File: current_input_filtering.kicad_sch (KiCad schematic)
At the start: 0 parts

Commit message: Launchpad controller revision 06/03/2024
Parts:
- added F14: Polyfuse, symbol Device:Polyfuse
- added J36: Conn_01x04_Socket, symbol Connector:Conn_01x04_Socket
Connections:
- net Iout: now also J36.2 (Pin_2)
- new net: F14.1, J36.1 (Pin_1)
- new net +12L: F14.2
- no-connect marks 0 -> 2
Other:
- note added: "super simple. fuse on the output to prevent damage by connecting to sketchy peripheral. sensor should drive the current, so shouldn't see too much noise => no filter required"

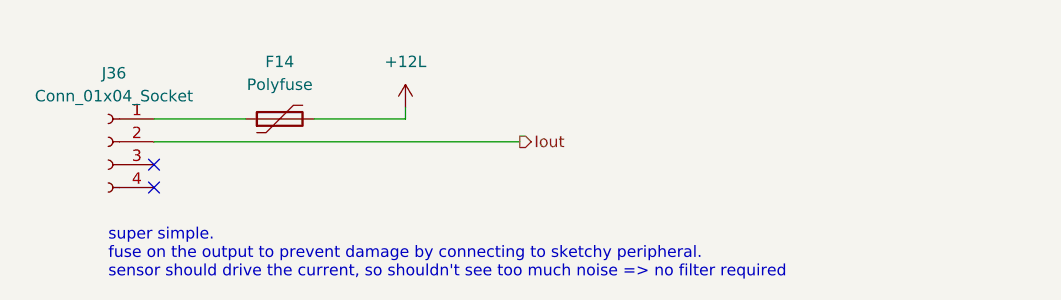
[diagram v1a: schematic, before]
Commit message: added footprints to almost all components
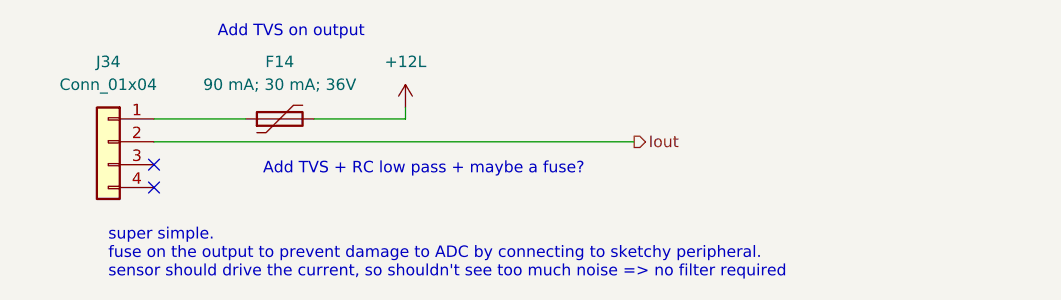
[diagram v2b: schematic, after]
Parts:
- removed J36: Conn_01x04_Socket, symbol Connector:Conn_01x04_Socket
- added J34: Conn_01x04, Connector_JST:JST_GH_BM04B-GHS-TBT_1x04-1MP_P1.25mm_Vertical, symbol Connector_Generic:Conn_01x04
- F14: value Polyfuse -> 90 mA; 30 mA; 36V; footprint (none) -> Fuse:Fuse_0805_2012Metric_Pad1.15x1.40mm_HandSolder; Mouser# (none) -> 576-0603L003/36YR
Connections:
- net Iout: now also J34.2 (Pin_2)
- net at F14.1: now also J34.1 (Pin_1)
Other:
- note added: "Add TVS + RC low pass + maybe a fuse?"
- note added: "Add TVS on output"
- note added: "super simple. fuse on the output to prevent damage to ADC by connecting to sketchy peripheral. sensor should drive the current, so shouldn't see too much noise => no filter required"
- note removed: "super simple. fuse on the output to prevent damage by connecting to sketchy peripheral. sensor should drive the current, so shouldn't see too much noise => no filter required"
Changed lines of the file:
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@@
 	(wire
 		(pts
-			(xy 100.33 60.96) (xy 59.69 60.96)
+			(xy 59.69 60.96) (xy 113.03 60.96)
 		)
 		(stroke
@@
 		)
 	)
-	(text "super simple. \nfuse on the output to prevent damage by connecting to sketchy peripheral.\nsensor should drive the current, so shouldn't see too much noise => no filter required"
+	(text "super simple. \nfuse on the output to prevent damage to ADC by connecting to sketchy peripheral.\nsensor should drive the current, so shouldn't see too much noise => no filter required"
 		(exclude_from_sim no)
 		(at 54.61 76.2 0)
@@
 		)
 	)
+	(text "Add TVS + RC low pass + maybe a fuse? "
+		(exclude_from_sim no)
+		(at 89.662 64.008 0)
+		(effects
+			(font
+				(size 1.27 1.27)
+			)
+		)
+	)
+	(text "Add TVS on output"
+		(exclude_from_sim no)
+		(at 74.93 48.768 0)
+		(effects
+			(font
+				(size 1.27 1.27)
+			)
+		)
+	)
 	(hierarchical_label "Iout"
 		(shape output)
-		(at 100.33 60.96 0)
+		(at 113.03 60.96 0)
 		(fields_autoplaced yes)
 		(effects
@@
 			)
 			(justify left)
-		)
-	)
-	(symbol
-		(lib_id "Connector:Conn_01x04_Socket")
-		(at 54.61 60.96 0)
-		(mirror y)
-		(unit 1)
-		(exclude_from_sim no)
-		(in_bom yes)
-		(on_board yes)
-		(dnp no)
-		(fields_autoplaced yes)
-		(property "Reference" "J36"
-			(at 55.245 53.34 0)
-			(effects
-				(font
-					(size 1.27 1.27)
-				)
-			)
-		)
-		(property "Value" "Conn_01x04_Socket"
-			(at 55.245 55.88 0)
-			(effects
-				(font
-					(size 1.27 1.27)
-				)
-			)
-		)
-		(property "Footprint" ""
-			(at 54.61 60.96 0)
-			(effects
-				(font
-					(size 1.27 1.27)
-				)
-				(hide yes)
-			)
-		)
-		(property "Datasheet" "~"
-			(at 54.61 60.96 0)
-			(effects
-				(font
-					(size 1.27 1.27)
-				)
-				(hide yes)
-			)
-		)
-		(property "Description" ""
-			(at 54.61 60.96 0)
-			(effects
-				(font
-					(size 1.27 1.27)
-				)
-				(hide yes)
-			)
-		)
-		(pin "1"
-		)
-		(pin "2"
-		)
-		(pin "3"
-		)
-		(pin "4"
-		)
-		(instances
-			(project "launchpad-controller-v2"
-				(path "/8b86c7a7-6364-4b1f-ab12-b4882a7d8ae2/dbac82f3-7447-480a-94cd-632941520571/8b7fdee2-3fcb-42fa-985c-bfd6e79c809e"
-					(reference "J36")
-					(unit 1)
-				)
-				(path "/8b86c7a7-6364-4b1f-ab12-b4882a7d8ae2/dbac82f3-7447-480a-94cd-632941520571/3919f185-a901-4bba-83cc-d41cbc978790"
-					(reference "J34")
-					(unit 1)
-				)
-				(path "/8b86c7a7-6364-4b1f-ab12-b4882a7d8ae2/dbac82f3-7447-480a-94cd-632941520571/72a8f92f-4182-43d4-8af1-acd53b109eaa"
-					(reference "J35")
-					(unit 1)
-				)
-				(path "/8b86c7a7-6364-4b1f-ab12-b4882a7d8ae2/dbac82f3-7447-480a-94cd-632941520571/ed57d8d7-5554-42ed-b519-c3d4f9c227b5"
-					(reference "J37")
-					(unit 1)
-				)
-				(path "/8b86c7a7-6364-4b1f-ab12-b4882a7d8ae2/5b962238-ad91-40ff-b76d-985e2dbc0aeb/ed57d8d7-5554-42ed-b519-c3d4f9c227b5"
-					(reference "J38")
-					(unit 1)
-				)
-				(path "/8b86c7a7-6364-4b1f-ab12-b4882a7d8ae2/5b962238-ad91-40ff-b76d-985e2dbc0aeb/8b7fdee2-3fcb-42fa-985c-bfd6e79c809e"
-					(reference "J39")
-					(unit 1)
-				)
-				(path "/8b86c7a7-6364-4b1f-ab12-b4882a7d8ae2/5b962238-ad91-40ff-b76d-985e2dbc0aeb/3919f185-a901-4bba-83cc-d41cbc978790"
-					(reference "J40")
-					(unit 1)
-				)
-				(path "/8b86c7a7-6364-4b1f-ab12-b4882a7d8ae2/5b962238-ad91-40ff-b76d-985e2dbc0aeb/72a8f92f-4182-43d4-8af1-acd53b109eaa"
-					(reference "J41")
-					(unit 1)
-				)
-			)
 		)
 	)
@@
 	)
 	(symbol
+		(lib_id "Connector_Generic:Conn_01x04")
+		(at 54.61 60.96 0)
+		(mirror y)
+		(unit 1)
+		(exclude_from_sim no)
+		(in_bom yes)
+		(on_board yes)
+		(dnp no)
+		(fields_autoplaced yes)
+		(property "Reference" "J34"
+			(at 54.61 52.07 0)
+			(effects
+				(font
+					(size 1.27 1.27)
+				)
+			)
+		)
+		(property "Value" "Conn_01x04"
+			(at 54.61 54.61 0)
+			(effects
+				(font
+					(size 1.27 1.27)
+				)
+			)
+		)
+		(property "Footprint" "Connector_JST:JST_GH_BM04B-GHS-TBT_1x04-1MP_P1.25mm_Vertical"
+			(at 54.61 60.96 0)
+			(effects
+				(font
+					(size 1.27 1.27)
+				)
+				(hide yes)
+			)
+		)
+		(property "Datasheet" "~"
+			(at 54.61 60.96 0)
+			(effects
+				(font
+					(size 1.27 1.27)
+				)
+				(hide yes)
+			)
+		)
+		(property "Description" "Generic connector, single row, 01x04, script generated (kicad-library-utils/schlib/autogen/connector/)"
+			(at 54.61 60.96 0)
+			(effects
+				(font
+					(size 1.27 1.27)
+				)
+				(hide yes)
+			)
+		)
+		(pin "1"
+		)
+		(pin "2"
+		)
+		(pin "4"
+		)
+		(pin "3"
+		)
+		(instances
+			(project "launchpad-controller-v2"
+				(path "/8b86c7a7-6364-4b1f-ab12-b4882a7d8ae2/5b962238-ad91-40ff-b76d-985e2dbc0aeb/ed57d8d7-5554-42ed-b519-c3d4f9c227b5"
+					(reference "J34")
+					(unit 1)
+				)
+				(path "/8b86c7a7-6364-4b1f-ab12-b4882a7d8ae2/dbac82f3-7447-480a-94cd-632941520571/3919f185-a901-4bba-83cc-d41cbc978790"
+					(reference "J14")
+					(unit 1)
+				)
+				(path "/8b86c7a7-6364-4b1f-ab12-b4882a7d8ae2/dbac82f3-7447-480a-94cd-632941520571/72a8f92f-4182-43d4-8af1-acd53b109eaa"
+					(reference "J17")
+					(unit 1)
+				)
+				(path "/8b86c7a7-6364-4b1f-ab12-b4882a7d8ae2/dbac82f3-7447-480a-94cd-632941520571/8b7fdee2-3fcb-42fa-985c-bfd6e79c809e"
+					(reference "J31")
+					(unit 1)
+				)
+				(path "/8b86c7a7-6364-4b1f-ab12-b4882a7d8ae2/dbac82f3-7447-480a-94cd-632941520571/ed57d8d7-5554-42ed-b519-c3d4f9c227b5"
+					(reference "J33")
+					(unit 1)
+				)
+				(path "/8b86c7a7-6364-4b1f-ab12-b4882a7d8ae2/5b962238-ad91-40ff-b76d-985e2dbc0aeb/8b7fdee2-3fcb-42fa-985c-bfd6e79c809e"
+					(reference "J35")
+					(unit 1)
+				)
+				(path "/8b86c7a7-6364-4b1f-ab12-b4882a7d8ae2/5b962238-ad91-40ff-b76d-985e2dbc0aeb/3919f185-a901-4bba-83cc-d41cbc978790"
+					(reference "J36")
+					(unit 1)
+				)
+				(path "/8b86c7a7-6364-4b1f-ab12-b4882a7d8ae2/5b962238-ad91-40ff-b76d-985e2dbc0aeb/72a8f92f-4182-43d4-8af1-acd53b109eaa"
+					(reference "J37")
+					(unit 1)
+				)
+			)
+		)
+	)
+	(symbol
 		(lib_id "Device:Polyfuse")
 		(at 73.66 58.42 90)
@@
 			)
 		)
-		(property "Value" "Polyfuse"
+		(property "Value" "90 mA; 30 mA; 36V"
 			(at 73.66 54.61 90)
 			(effects
@@
 			)
 		)
-		(property "Footprint" ""
+		(property "Footprint" "Fuse:Fuse_0805_2012Metric_Pad1.15x1.40mm_HandSolder"
 			(at 78.74 57.15 0)
 			(effects
@@
 			)
 		)
-		(property "Datasheet" "~"
+		(property "Datasheet" "https://m.littelfuse.com/media?resourcetype=datasheets&itemid=879563f9-97a7-4e71-adba-37de085b333f&filename=littelfuse-ptc-0603l-datasheet"
 			(at 73.66 58.42 0)
 			(effects
@@
 			)
 		)
-		(property "Description" ""
+		(property "Description" "0603L003/36YR"
 			(at 73.66 58.42 0)
 			(effects
+				(font
+					(size 1.27 1.27)
+				)
+				(hide yes)
+			)
+		)
+		(property "LCSC#" ""
+			(at 73.66 58.42 0)
+			(effects
+				(font
+					(size 1.27 1.27)
+				)
+				(hide yes)
+			)
+		)
+		(property "Mouser#" "576-0603L003/36YR"
+			(at 73.66 58.42 0)
+			(effects
